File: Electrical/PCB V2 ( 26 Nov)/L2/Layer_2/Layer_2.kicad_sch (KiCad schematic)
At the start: 38 parts, among them J1 Conn_01x02, Q1 AON6354, SW1 SW_Push, U1 LM2596ADJ, U12 VNH5019ATR-E, U2 LM2596ADJ, U3 XT30UPB-M, U4 XT30UPB-M, U5 ESP32-S3-DEVKITM-1-N8

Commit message: updated motor 1 controller cos cx
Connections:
- net Motor 1 ENB is gone; now on net Motor 1 ENA: R4.1, R7.1
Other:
- moved on the sheet: Q1, R6, R7, R8
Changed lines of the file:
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@@
 	)
 	(junction
-		(at 39.37 157.48)
+		(at 107.95 142.24)
 		(diameter 0)
 		(color 0 0 0 0)
 	)
 	(junction
-		(at 107.95 142.24)
+		(at 36.83 137.16)
 		(diameter 0)
 		(color 0 0 0 0)
@@
 	)
 	(junction
+		(at 36.83 157.48)
+		(diameter 0)
+		(color 0 0 0 0)
+	)
+	(junction
 		(at 107.95 156.21)
 		(diameter 0)
@@
 	(wire
 		(pts
-			(xy 31.75 134.62) (xy 31.75 137.16)
-		)
-		(stroke
-			(width 0)
-			(type default)
-		)
-	)
-	(wire
-		(pts
 			(xy 104.14 156.21) (xy 107.95 156.21)
 		)
@@
 	(wire
 		(pts
-			(xy 86.36 137.16) (xy 92.71 137.16)
+			(xy 86.36 137.16) (xy 96.52 137.16)
 		)
 		(stroke
@@
 	(wire
 		(pts
-			(xy 39.37 157.48) (xy 30.48 157.48)
+			(xy 107.95 156.21) (xy 111.76 156.21)
 		)
 		(stroke
@@
 	(wire
 		(pts
-			(xy 107.95 156.21) (xy 111.76 156.21)
+			(xy 36.83 168.91) (xy 86.36 168.91)
 		)
 		(stroke
@@
 	(wire
 		(pts
-			(xy 39.37 168.91) (xy 86.36 168.91)
+			(xy 36.83 157.48) (xy 27.94 157.48)
 		)
 		(stroke
@@
 	(wire
 		(pts
-			(xy 31.75 124.46) (xy 31.75 127)
+			(xy 31.75 124.46) (xy 31.75 129.54)
 		)
 		(stroke
@@
 	(wire
 		(pts
-			(xy 31.75 137.16) (xy 43.18 137.16)
+			(xy 31.75 137.16) (xy 36.83 137.16)
 		)
 		(stroke
@@
 	(wire
 		(pts
+			(xy 36.83 137.16) (xy 43.18 137.16)
+		)
+		(stroke
+			(width 0)
+			(type default)
+		)
+	)
+	(wire
+		(pts
+			(xy 36.83 157.48) (xy 43.18 157.48)
+		)
+		(stroke
+			(width 0)
+			(type default)
+		)
+	)
+	(wire
+		(pts
 			(xy 86.36 168.91) (xy 86.36 165.1)
 		)
@@
 	(wire
 		(pts
-			(xy 39.37 157.48) (xy 39.37 160.02)
+			(xy 36.83 157.48) (xy 36.83 160.02)
 		)
 		(stroke
@@
 	(wire
 		(pts
-			(xy 25.4 139.7) (xy 36.83 139.7)
+			(xy 27.94 139.7) (xy 36.83 139.7)
 		)
 		(stroke
@@
 	(wire
 		(pts
-			(xy 39.37 168.91) (xy 39.37 167.64)
+			(xy 36.83 168.91) (xy 36.83 167.64)
 		)
 		(stroke
@@
 	(wire
 		(pts
-			(xy 90.17 132.08) (xy 100.33 132.08)
+			(xy 90.17 132.08) (xy 104.14 132.08)
 		)
 		(stroke
@@
 	(wire
 		(pts
-			(xy 39.37 157.48) (xy 43.18 157.48)
+			(xy 27.94 149.86) (xy 43.18 149.86)
 		)
 		(stroke
@@
 	(wire
 		(pts
-			(xy 26.67 137.16) (xy 31.75 137.16)
+			(xy 16.51 48.26) (xy 29.21 48.26)
 		)
 		(stroke
@@
 	(wire
 		(pts
-			(xy 25.4 149.86) (xy 43.18 149.86)
+			(xy 27.94 137.16) (xy 31.75 137.16)
 		)
 		(stroke
@@
 	(wire
 		(pts
-			(xy 16.51 48.26) (xy 29.21 48.26)
+			(xy 36.83 124.46) (xy 36.83 129.54)
 		)
 		(stroke
@@
 	(wire
 		(pts
-			(xy 36.83 124.46) (xy 36.83 132.08)
+			(xy 104.14 142.24) (xy 107.95 142.24)
 		)
 		(stroke
@@
 	(wire
 		(pts
-			(xy 100.33 142.24) (xy 107.95 142.24)
+			(xy 27.94 144.78) (xy 43.18 144.78)
 		)
 		(stroke
@@
 	(wire
 		(pts
-			(xy 25.4 144.78) (xy 43.18 144.78)
+			(xy 107.95 129.54) (xy 107.95 142.24)
 		)
 		(stroke
@@
 	(wire
 		(pts
-			(xy 107.95 129.54) (xy 107.95 142.24)
+			(xy 31.75 124.46) (xy 36.83 124.46)
 		)
 		(stroke
@@
 	(wire
 		(pts
-			(xy 31.75 124.46) (xy 36.83 124.46)
+			(xy 107.95 163.83) (xy 107.95 165.1)
 		)
 		(stroke
@@
 	(wire
 		(pts
-			(xy 107.95 163.83) (xy 107.95 165.1)
+			(xy 36.83 137.16) (xy 36.83 139.7)
 		)
 		(stroke
@@
 	(hierarchical_label "Pwm Motor 1"
 		(shape input)
-		(at 30.48 157.48 180)
+		(at 27.94 157.48 180)
 		(fields_autoplaced yes)
 		(effects
@@
 	(hierarchical_label "Motor 1 ENA"
 		(shape input)
-		(at 26.67 137.16 180)
+		(at 27.94 137.16 180)
 		(fields_autoplaced yes)
 		(effects
@@
 	(hierarchical_label "Motor 1 In B"
 		(shape input)
-		(at 25.4 149.86 180)
+		(at 27.94 149.86 180)
 		(fields_autoplaced yes)
 		(effects
@@
 	(hierarchical_label "Motor 1 In A"
 		(shape input)
-		(at 25.4 144.78 180)
+		(at 27.94 144.78 180)
 		(fields_autoplaced yes)
 		(effects
@@
 	(hierarchical_label "Motor 1 ENB"
 		(shape input)
-		(at 25.4 139.7 180)
+		(at 27.94 139.7 180)
 		(fields_autoplaced yes)
 		(effects
@@
 	(symbol
 		(lib_id "Device:R")
-		(at 36.83 135.89 180)
+		(at 36.83 133.35 180)
 		(unit 1)
 		(exclude_from_sim no)
@@
 		(dnp no)
 		(property "Reference" "R7"
-			(at 39.37 134.62 0)
+			(at 39.37 132.08 0)
 			(effects
 				(font
@@
 		)
 		(property "Value" "3K3"
-			(at 39.37 137.16 0)
+			(at 39.37 134.62 0)
 			(effects
 				(font
@@
 		)
 		(property "Footprint" "2024l2:res0603"
-			(at 38.608 135.89 90)
+			(at 38.608 133.35 90)
 			(effects
 				(font
@@
 		)
 		(property "Datasheet" "~"
-			(at 36.83 135.89 0)
+			(at 36.83 133.35 0)
 			(effects
 				(font
@@
 		)
 		(property "Description" ""
-			(at 36.83 135.89 0)
+			(at 36.83 133.35 0)
 			(effects
 				(font
@@
 	(symbol
 		(lib_id "vincent:AON6354")
-		(at 92.71 137.16 0)
+		(at 96.52 137.16 0)
 		(mirror x)
 		(unit 1)
@@
 		(fields_autoplaced yes)
 		(property "Reference" "Q1"
-			(at 104.14 135.8899 0)
+			(at 107.95 135.8899 0)
 			(effects
 				(font
@@
 		)
 		(property "Value" "AON6354"
-			(at 104.14 138.4299 0)
+			(at 107.95 138.4299 0)
 			(effects
 				(font
@@
 		)
 		(property "Footprint" "2024l2:8-DFN (5x6)"
-			(at 100.33 134.62 90)
+			(at 104.14 134.62 90)
 			(effects
 				(font
@@
 		)
 		(property "Datasheet" "https://aosmd.com/res/data_sheets/AON6354.pdf"
-			(at 100.33 137.16 0)
+			(at 104.14 137.16 0)
 			(effects
 				(font
@@
 		)
 		(property "Description" ""
-			(at 92.71 137.16 0)
+			(at 96.52 137.16 0)
 			(effects
 				(font
@@
 	(symbol
 		(lib_id "Device:R")
-		(at 39.37 163.83 0)
+		(at 36.83 163.83 0)
 		(unit 1)
 		(exclude_from_sim no)
@@
 		(fields_autoplaced yes)
 		(property "Reference" "R6"
-			(at 41.91 162.5599 0)
+			(at 39.37 162.5599 0)
 			(effects
 				(font
@@
 		)
 		(property "Value" "10K"
-			(at 41.91 165.0999 0)
+			(at 39.37 165.0999 0)
 			(effects
 				(font
@@
 		)
 		(property "Footprint" "2024l2:res0603"
-			(at 37.592 163.83 90)
+			(at 35.052 163.83 90)
 			(effects
 				(font
@@
 		)
 		(property "Datasheet" "~"
-			(at 39.37 163.83 0)
+			(at 36.83 163.83 0)
 			(effects
 				(font
@@
 		)
 		(property "Description" ""
-			(at 39.37 163.83 0)
+			(at 36.83 163.83 0)
 			(effects
 				(font
@@
 	(symbol
 		(lib_id "Device:R")
-		(at 31.75 130.81 180)
+		(at 31.75 133.35 180)
 		(unit 1)
 		(exclude_from_sim no)
@@
 		(dnp no)
 		(property "Reference" "R8"
-			(at 34.29 129.54 0)
+			(at 34.29 132.08 0)
 			(effects
 				(font
@@
 		)
 		(property "Value" "3K3"
-			(at 34.29 132.08 0)
+			(at 34.29 134.62 0)
 			(effects
 				(font
@@
 		)
 		(property "Footprint" "2024l2:res0603"
-			(at 33.528 130.81 90)
+			(at 33.528 133.35 90)
 			(effects
 				(font
@@
 		)
 		(property "Datasheet" "~"
-			(at 31.75 130.81 0)
+			(at 31.75 133.35 0)
 			(effects
 				(font
@@
 		)
 		(property "Description" ""
-			(at 31.75 130.81 0)
+			(at 31.75 133.35 0)
 			(effects
 				(font

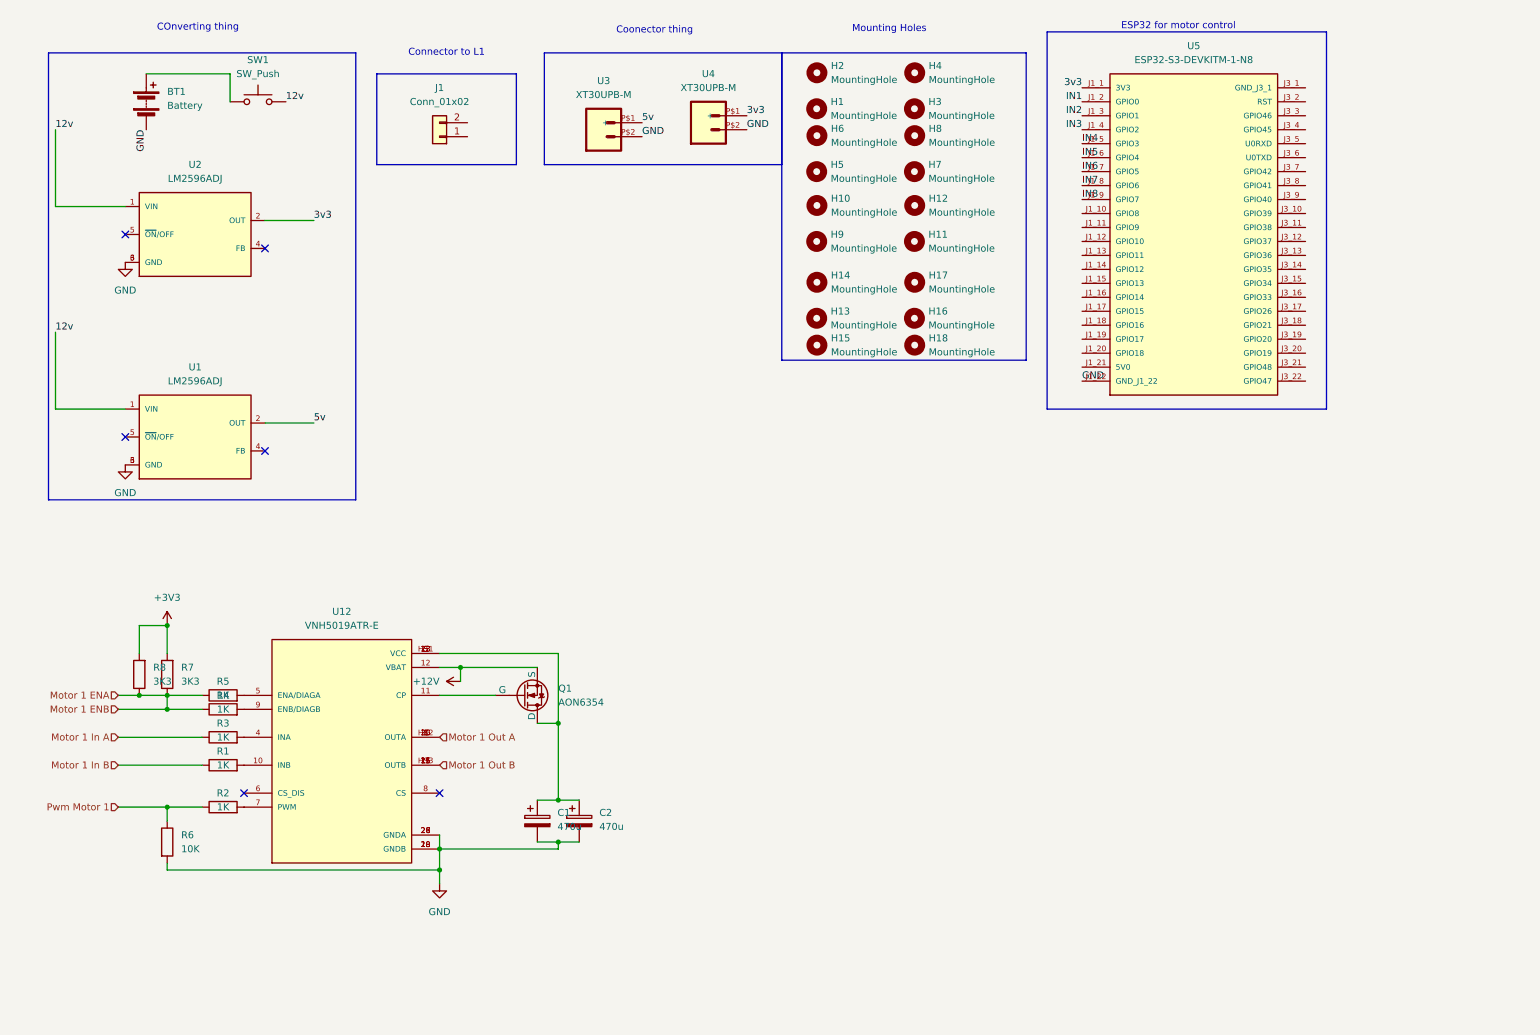
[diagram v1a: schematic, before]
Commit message: re arragngedn schematic
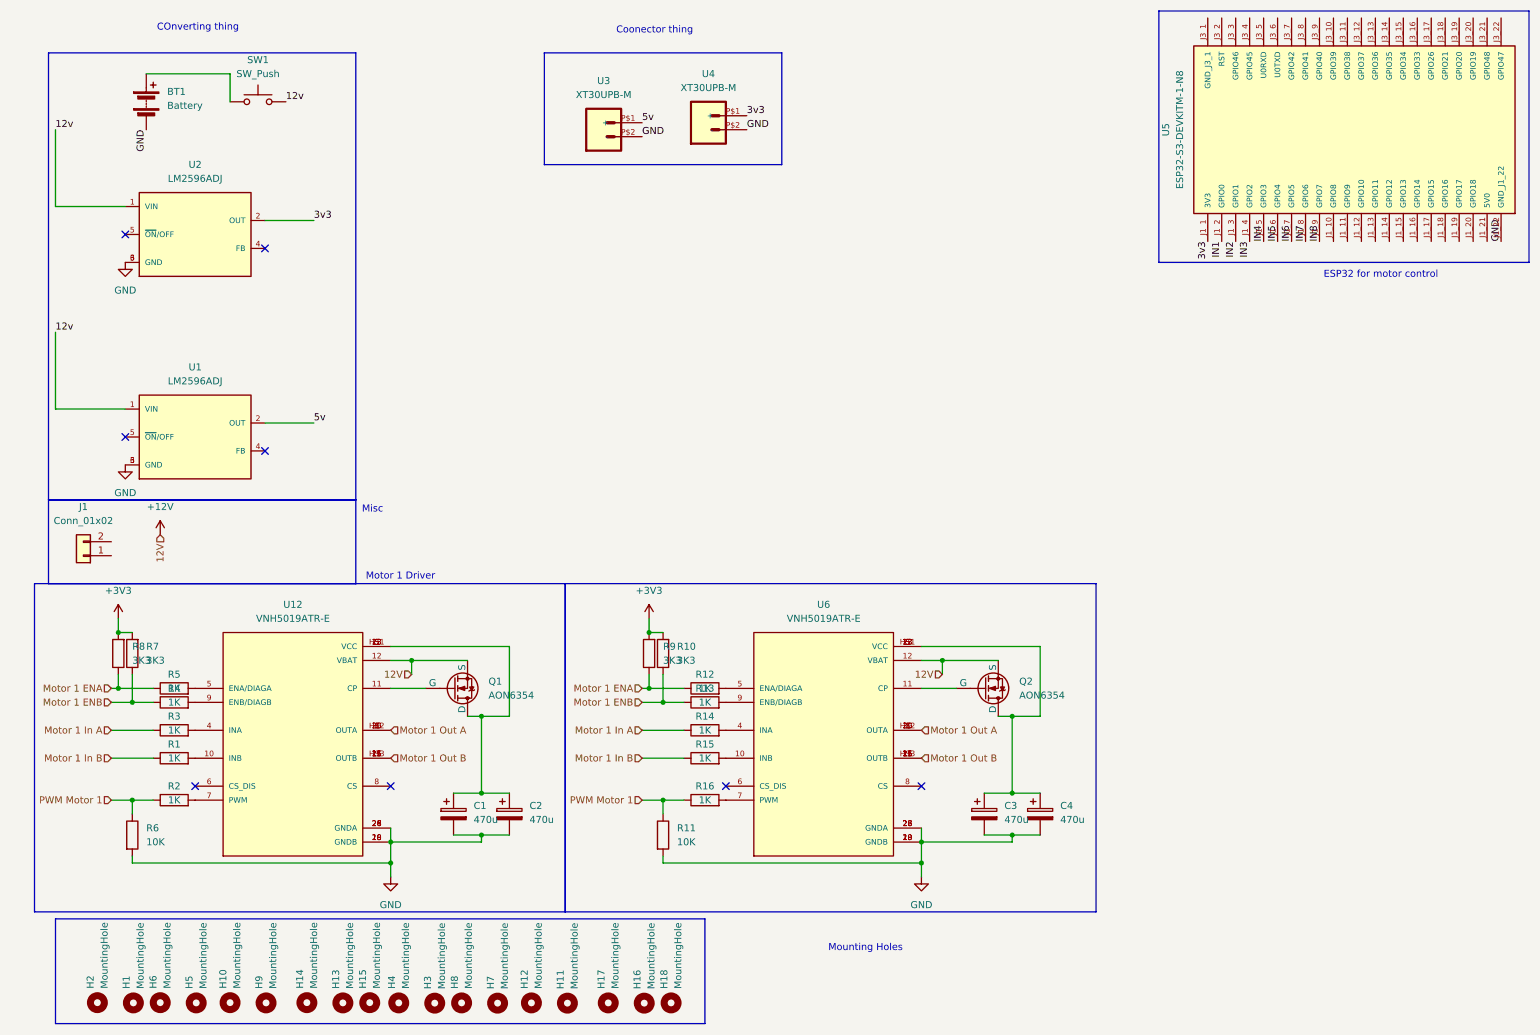
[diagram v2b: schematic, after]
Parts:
- added C3, C4: 470u, 2024l2:CP_Radial_D8.0mm_P3.50mm, symbol Device:C_Polarized
- added Q2: AON6354, 2024l2:8-DFN (5x6), symbol vincent:AON6354
- added R10, R9: 3K3, 2024l2:res0603, symbol Device:R
- added R11: 10K, 2024l2:res0603, symbol Device:R
- added R12, R13, R14, R15, R16: 1K, 2024l2:res0603, symbol Device:R
- added U6: VNH5019ATR-E, VNH5019ATR-E:IC_VNH5019ATR-E, symbol VHN5019ATR-E:VNH5019ATR-E
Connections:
- net +12V: now also Q2.1 (S), Q2.2 (S), Q2.3 (S), U6.12 (VBAT)
- net +3V3: now also R10.2, R9.2
- net GND: now also C3.2, C4.2, R11.2, U6.18 (GNDB), U6.19 (GNDB), U6.20 (GNDB), U6.26 (GNDA), U6.27 (GNDA), U6.28 (GNDA)
- net Motor 1 ENA: now also R12.1, R9.1; no longer R4.1, R7.1
- net Motor 1 In A: now also R14.1
- net Motor 1 In B: now also R15.1
- net Motor 1 Out A: now also U6.1 (OUTA), U6.25 (OUTA), U6.30 (OUTA), U6.HS2 (OUTA)
- net Motor 1 Out B: now also U6.15 (OUTB), U6.16 (OUTB), U6.21 (OUTB), U6.HS3 (OUTB)
- net Pwm Motor 1 renamed PWM Motor 1
- net PWM Motor 1: now also R11.1, R16.1
- new net: R16.2, U6.7 (PWM)
- new net: R15.2, U6.10 (INB)
- new net: Q2.4 (G), U6.11 (CP)
- new net: C3.1, C4.1, Q2.5 (D), Q2.6 (D), Q2.7 (D), Q2.8 (D), Q2.9 (D), U6.13 (VCC), U6.23 (VCC), U6.3 (VCC), U6.HS1 (VCC)
- new net: R14.2, U6.4 (INA)
- new net: R12.2, U6.5 (ENA/DIAGA)
- new net: R13.2, U6.9 (ENB/DIAGB)
- new net Motor 1 ENB: R10.1, R13.1, R4.1, R7.1
- no-connect marks 6 -> 8
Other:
- note added: "Misc"
- note added: "Motor 1 Driver"
- note removed: "Connector to L1"
- moved on the sheet: C1, C2, H1, H10, H11, H12, H13, H14, H15, H16, H17, H18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
